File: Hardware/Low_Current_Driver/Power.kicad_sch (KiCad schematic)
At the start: 22 parts, among them SW1 SW_DPST, U4 TPS7A470x, U5 TPS7A470x, U6 TPS7A33

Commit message: Checkpoint before channel-replication refactor
Snapshot of schematic/PCB work-in-progress prior to restructuring
Channel_Outputs into a reusable hierarchical channel sheet for
replicate-layout. Adds DPST relay footprint.

Co-Authored-By: Claude Opus 4.8 <noreply@anthropic.com>
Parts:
- SW1: footprint (none) -> fieldZero:DPST_RA83231100; DigiKey https://www.digikey.com/en/products/detail/e-switch/RA83231100/EG5682-ND -> https://www.digikey.com/en/products/detail/e-switch/RA83231100/8540806
- TP1, TP2: footprint (none) -> TestPoint:TestPoint_Pad_D1.0mm
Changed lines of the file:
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@@
 			)
 		)
-		(property "Footprint" ""
+		(property "Footprint" "TestPoint:TestPoint_Pad_D1.0mm"
 			(at 72.39 30.48 0)
 			(hide yes)
@@
 			)
 		)
-		(property "Footprint" ""
+		(property "Footprint" "TestPoint:TestPoint_Pad_D1.0mm"
 			(at 67.31 40.64 0)
 			(hide yes)
@@
 			)
 		)
-		(property "Footprint" ""
+		(property "Footprint" "fieldZero:DPST_RA83231100"
 			(at 41.91 33.02 0)
 			(hide yes)
@@
 			)
 		)
-		(property "DigiKey" "https://www.digikey.com/en/products/detail/e-switch/RA83231100/EG5682-ND"
-			(at 41.91 33.02 0)
-			(hide yes)
+		(property "DigiKey" "https://www.digikey.com/en/products/detail/e-switch/RA83231100/8540806"
+			(at 41.91 33.02 0)
+			(hide yes)

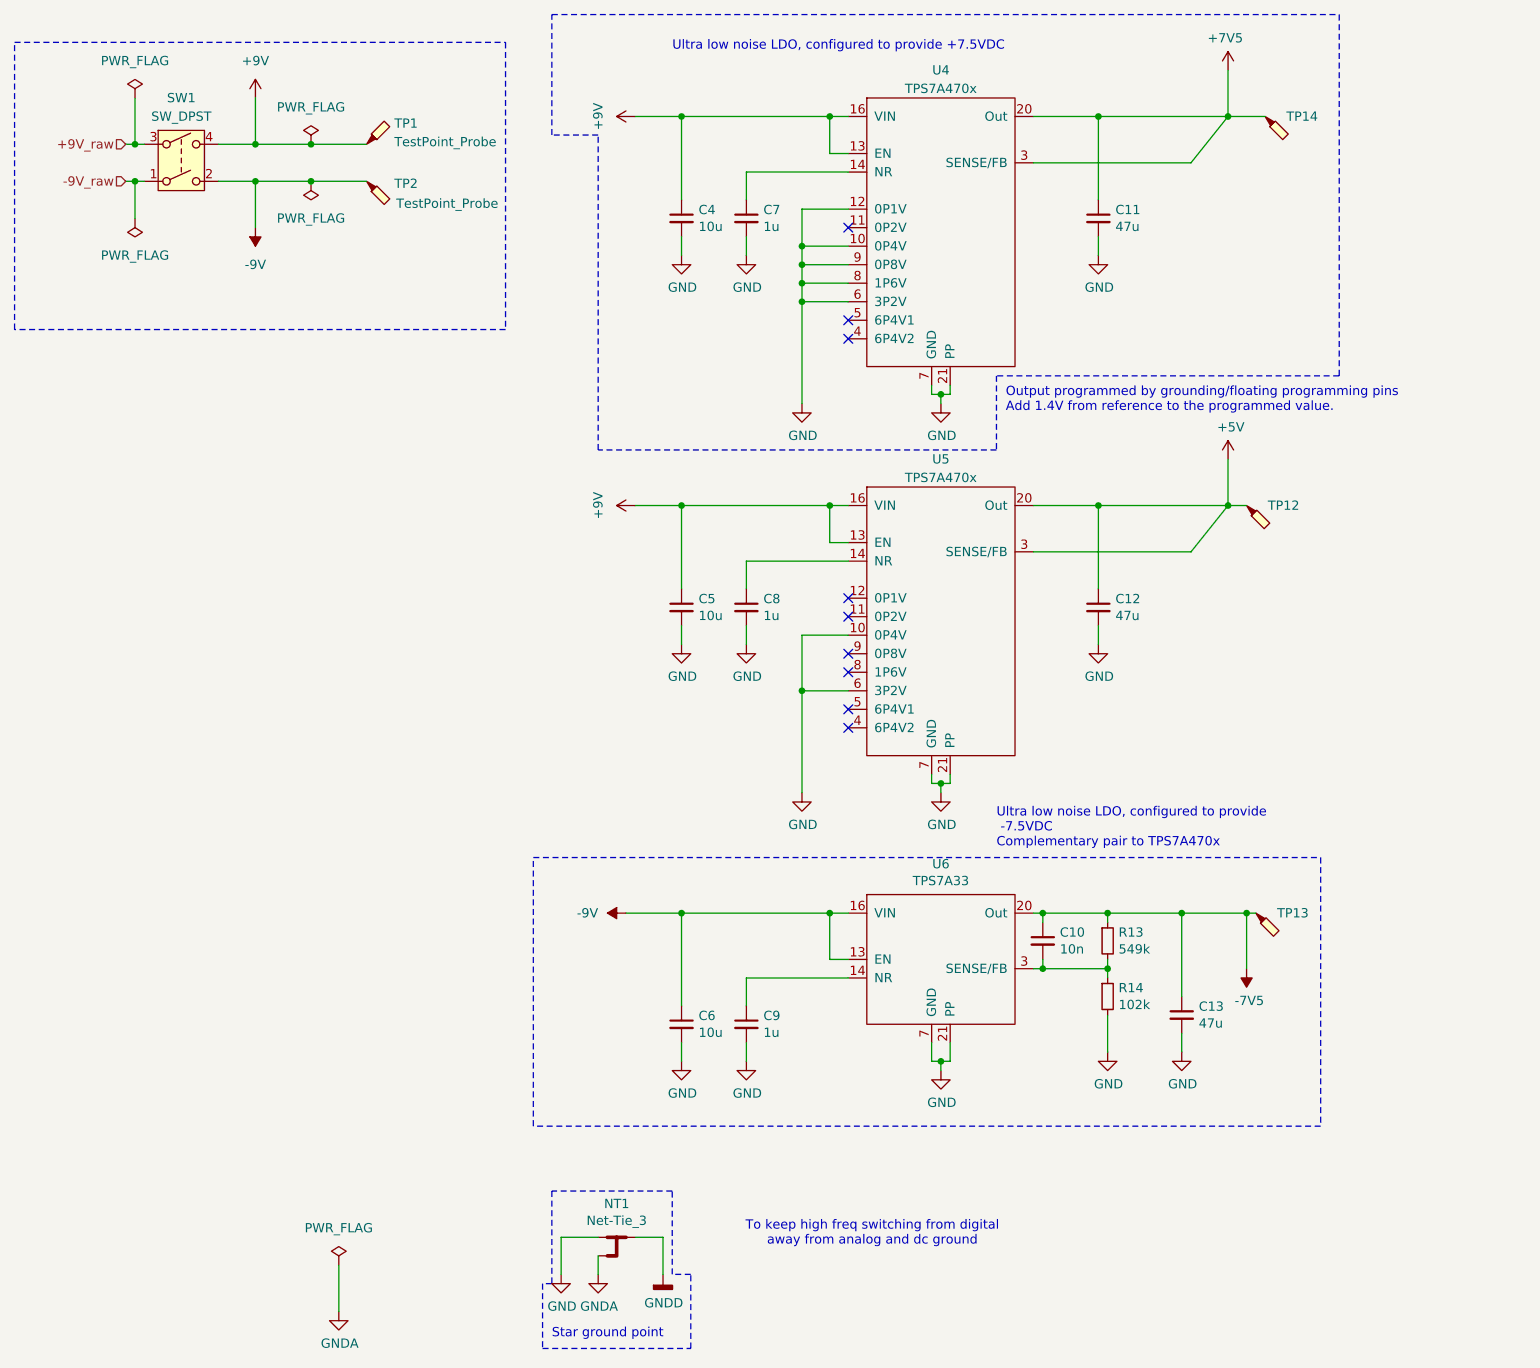
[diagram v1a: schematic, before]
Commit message: Replicate coil drive channel via native multichannel sheets
Root schematic now instantiates Channel_Outputs.kicad_sch twice as
Coil_Drive_A / Coil_Drive_B, with DAC_OPA.kicad_sch added as a sub-sheet
of DAC.kicad_sch (also instantiated twice). PCB relaid out to match.

Also drops the abandoned ESP32-S3 leftovers (footprint file and the
sym-lib-table entry pointing at an absolute path), removes the stale
Low_Current_Driver-cache legacy lib entry, and adds the STEP models
referenced by the board under 3DModels/.

Co-Authored-By: Claude Opus 4.8 <noreply@anthropic.com>
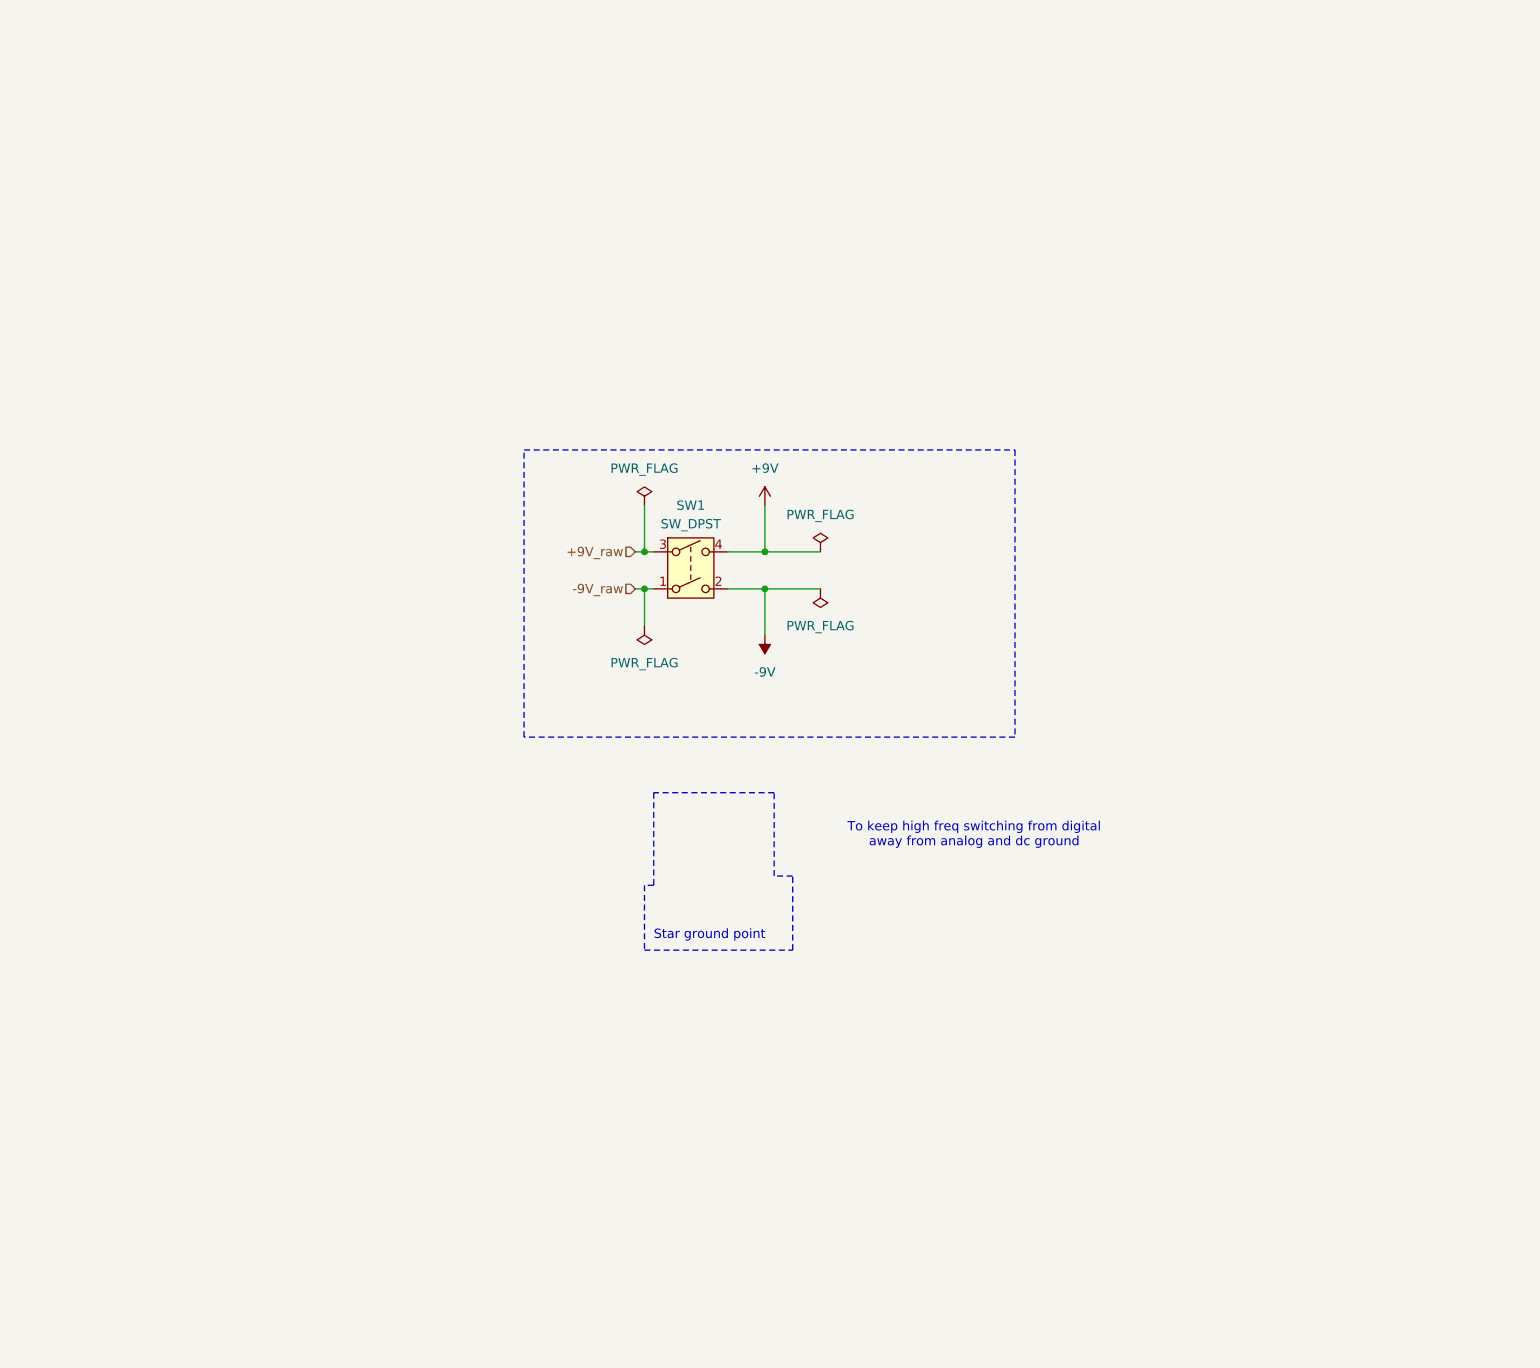
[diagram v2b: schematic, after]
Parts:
- removed C10: 10n, Capacitor_SMD:C_0603_1608Metric_Pad1.08x0.95mm_HandSolder, symbol Device:C_Small
- removed C11, C12, C13: 47u, Capacitor_SMD:C_1210_3225Metric_Pad1.33x2.70mm_HandSolder, symbol Device:C_Small
- removed C4, C5, C6: 10u, Capacitor_SMD:C_1206_3216Metric_Pad1.33x1.80mm_HandSolder, symbol Device:C_Small
- removed C7, C8, C9: 1u, Capacitor_SMD:C_0603_1608Metric_Pad1.08x0.95mm_HandSolder, symbol Device:C_Small
- removed NT1: Net-Tie_3, NetTie:NetTie-3_SMD_Pad2.0mm, symbol Device:Net-Tie_3
- removed R13: 549k, Resistor_SMD:R_0603_1608Metric_Pad0.98x0.95mm_HandSolder, symbol Device:R_Small
- removed R14: 102k, Resistor_SMD:R_0603_1608Metric_Pad0.98x0.95mm_HandSolder, symbol Device:R_Small
- removed TP1, TP12, TP13, TP14, TP2: TestPoint_Probe, TestPoint:TestPoint_Pad_D1.0mm, symbol Connector:TestPoint_Probe
- removed U4, U5: TPS7A470x, Package_DFN_QFN:QFN-20-1EP_5x5mm_P0.65mm_EP3.35x3.35mm_ThermalVias, symbol vernier_current_driver:TPS7A470x
- removed U6: TPS7A33, Package_DFN_QFN:QFN-20-1EP_5x5mm_P0.65mm_EP3.35x3.35mm_ThermalVias, symbol vernier_current_driver:TPS7A33
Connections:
- no-connect marks 9 -> 0
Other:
- note removed: "Output programmed by grounding/floating programming pins Add 1.4V from reference to the programmed value."
- note removed: "Ultra low noise LDO, configured to provide +7.5VDC"
- note removed: "Ultra low noise LDO, configured to provide -7.5VDC Complementary pair to TPS7A470x"
- company: Strathclyde University -> QUBIC MEG Lab
- title: "Vernier" Low Current Driver - LCD -> FieldZero Coil Driver - Low Current Driver (2 ch, +/-10 mA)
- moved on the sheet: SW1
